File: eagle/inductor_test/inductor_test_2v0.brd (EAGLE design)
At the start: 25.4 x 25.4 mm, 43 parts, among them U1 OPA2369, U3 SC70, U4 SOT-23-6, U5 TSSOP-14

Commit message: added all components for inductor inspector
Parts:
- removed U$1: (no value), powerfilm:NEMA_1-15_TIGHT
- added C15: (no value), rcl:C0402
- added R20, R21, R22, R23: (no value), rcl:R0402
- added TP1, TP10, TP11, TP12, TP13, TP14, TP2, TP3, TP4, TP5, TP6, TP7, TP8, TP9: TP_MULT, skyspecs:TP_MULT
- added U$2: (no value), powerfilm:NEMA_F2
- added U2: OPA2369, powerfilm:SOT-23-8
- C3: device rcl:C0603 -> rcl:C0402
- moved C2 174.2 mm to (50.8, 6.11), turned to 180 degrees
- moved R5 148.3 mm to (12.7, 3.81), turned to 270 degrees
- moved C1 142.5 mm to (-1.27, 5.08), turned to 90 degrees
- moved R4 127.5 mm to (3.81, -6.35), turned to 90 degrees
- moved R2 123.8 mm to (-1.27, 0.00), turned to 90 degrees
- moved R3 123.5 mm to (2.54, -6.35), turned to 90 degrees
- moved R7 105.1 mm to (50.8, 7.38), turned to 180 degrees
- moved U3 104.7 mm to (50.8, 10.2)
- moved R6 103.1 mm to (50.8, 8.57)
- moved C3 103.0 mm to (51.4, 11.7), turned to 180 degrees
- moved L1 8.89 mm to (4.45, 5.08), turned to 226.6 degrees
- moved L2 7.21 mm to (3.61, 1.27), turned to 262.9 degrees
- moved L3 7.11 mm to (3.56, -2.54), turned to 284.7 degrees
- moved L4 4.06 mm to (2.03, 4.83), turned to 255.1 degrees
- moved L5 3.05 mm to (1.52, 0.00)
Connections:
- new net N$13: R22.1, R23.2, U2.P5
- new net N$16: R20.2, R21.1, U2.P3
- net +3V3: now also C15.1, R21.2, R22.2, U2.P8
- net GND: now also C15.2, R20.1, R23.1, TP10.P$1, TP11.P$1, TP12.P$1, TP13.P$1, TP14.P$1, TP9.P$1, U2.P4
- net OUT1_SC70: now also TP1.P$1
- net OUT1_SOT23: now also TP3.P$1
- net OUT1_TSSOP14: now also TP5.P$1
- net OUT2_SC70: now also TP2.P$1
- net OUT2_SOT23: now also TP4.P$1
- net OUT2_TSSOP14: now also TP6.P$1
- net VREF_1V65: now also TP7.P$1, U2.P1, U2.P2
- net VREF_V054: now also TP8.P$1, U2.P6, U2.P7
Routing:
- net L1P2: track 42.8 -> 0.00 mm
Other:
- board size 25.4 x 25.4 mm -> 25.4 x 50.8 mm
- board text removed: "1"
- board text removed: "10"
- board text removed: "11"
- board text removed: "12"
- board text removed: "13"
- board text removed: "14"
- board text removed: "15"
- board text removed: "2"
- board text removed: "3"
- board text removed: "4"
- board text removed: "5"
- board text removed: "6"
- board text removed: "7"
- board text removed: "8"
- board text removed: "9"
- board text removed: "CONTROL"
- board text removed: "LOAD"
- board text removed: "Layout:"

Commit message: all components added for inductor inspector
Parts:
- removed TP14: TP_MULT, skyspecs:TP_MULT
- added C16: 22pF, rcl:C0402_SM
- added C17: 4.7uF, rcl:C0402_SM
- added C18, C19: 0.1uF, rcl:C0402_SM
- added C20, C21: 22uF, rcl:C0603_SM
- added C22: 0.1uF, rcl:C0603
- added J1: MA02-1, con-lstb:MA02-1_MOLEX-TH
- added L6: 10uH, rcl:L0805
- added R24: 560k, rcl:R0402_SM
- added R25: 180k, rcl:R0402_SM
- added R26: 1 1%, rcl:R0603_SM
- added R27, R28: 10k, rcl:R0603
- added R29, R30: 10, rcl:R0603
- added TP16: TP_MULT, skyspecs:TP_MULT
- added U6: TPS62122, powerfilm:WDFN-6
- added U7: MAX9910, powerfilm:SC70-5
- C14, C4, C5: device rcl:C0603 -> rcl:C0402
- moved TP9 281.2 mm to (35.6, 10.8)
- moved TP12 280.6 mm to (35.6, -8.89)
- moved TP11 278.5 mm to (35.6, -4.76)
- moved TP10 276.3 mm to (35.6, -0.64)
- moved TP13 275.7 mm to (35.6, -20.3)
- moved TP4 243.3 mm to (35.6, 3.17)
- moved TP2 242.1 mm to (35.6, 14.6)
- moved TP3 240.9 mm to (35.6, 6.99)
- moved TP1 239.6 mm to (35.6, 18.4)
- moved TP8 237.8 mm to (35.6, -27.9)
- moved TP6 236.6 mm to (35.6, -16.5)
- moved TP7 235.4 mm to (35.6, -24.1)
- moved TP5 234.2 mm to (35.6, -12.7)
- moved C14 213.4 mm to (27.0, 0.48), turned to 270 degrees
- moved C12 204.8 mm to (28.5, 6.03)
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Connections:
- new net N$19: C16.2, R24.1, R25.2, U6.P3
- new net N$20: L6.2, U6.P1
- new net N$21: R28.1, R29.2, U7.P1
- new net N$22: R27.1, R30.2, U7.P3
- new net N$23: R27.2, TP16.P$1, U7.P4
- new net VCC: C17.1, C18.1, J1.P1, U6.P4, U6.P5
- new net VS+: C16.1, C19.1, C20.1, L6.1, R24.2, R26.1, R29.1, U6.P2
- net +3V3: now also C21.1, C22.1, R26.2, R30.1, U7.P5
- net GND: now also C17.2, C18.2, C19.2, C20.2, C21.2, C22.2, J1.P2, R25.1, R28.2, U6.P6, U6.PAD, U7.P2; no longer TP14.P$1
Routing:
- added copper zone on layer 1, net GND
- added copper zone on layer 16, net GND
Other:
- outline, holes or cut-outs redrawn

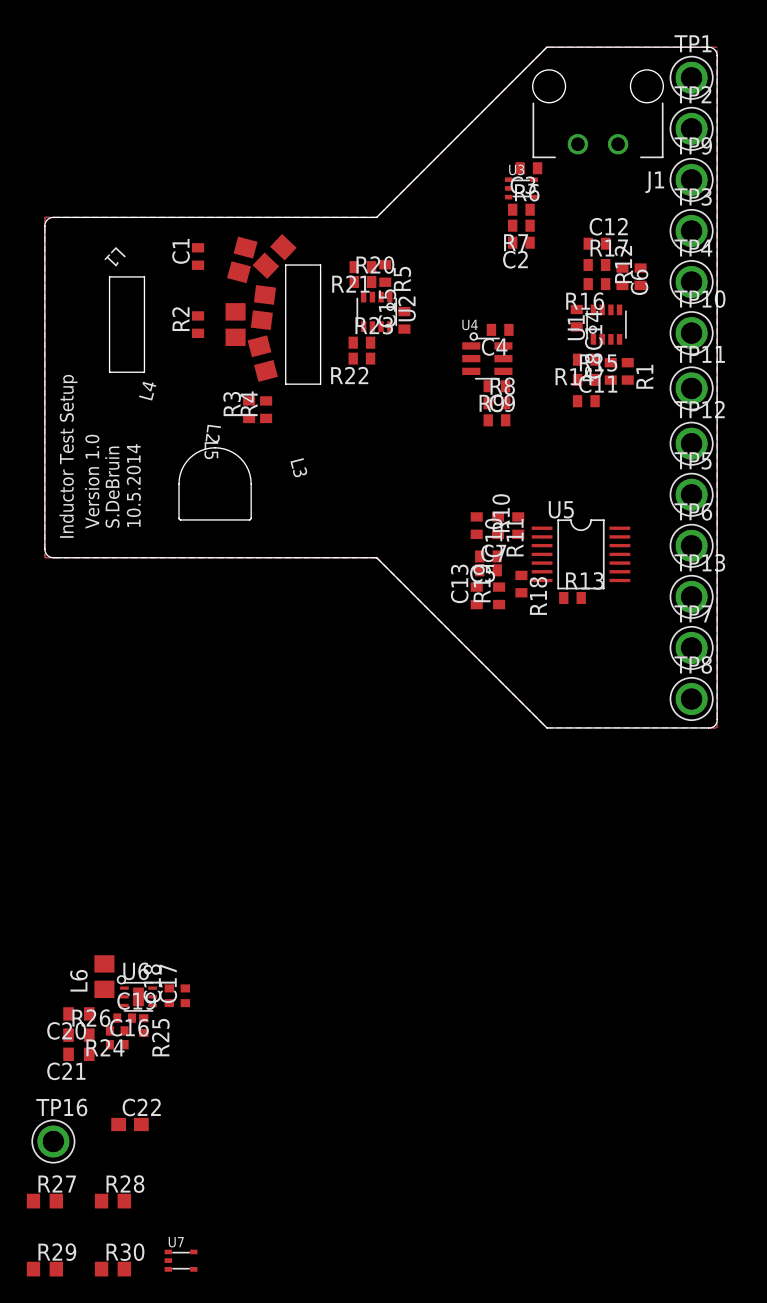
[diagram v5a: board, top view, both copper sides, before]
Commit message: 23 airwires left
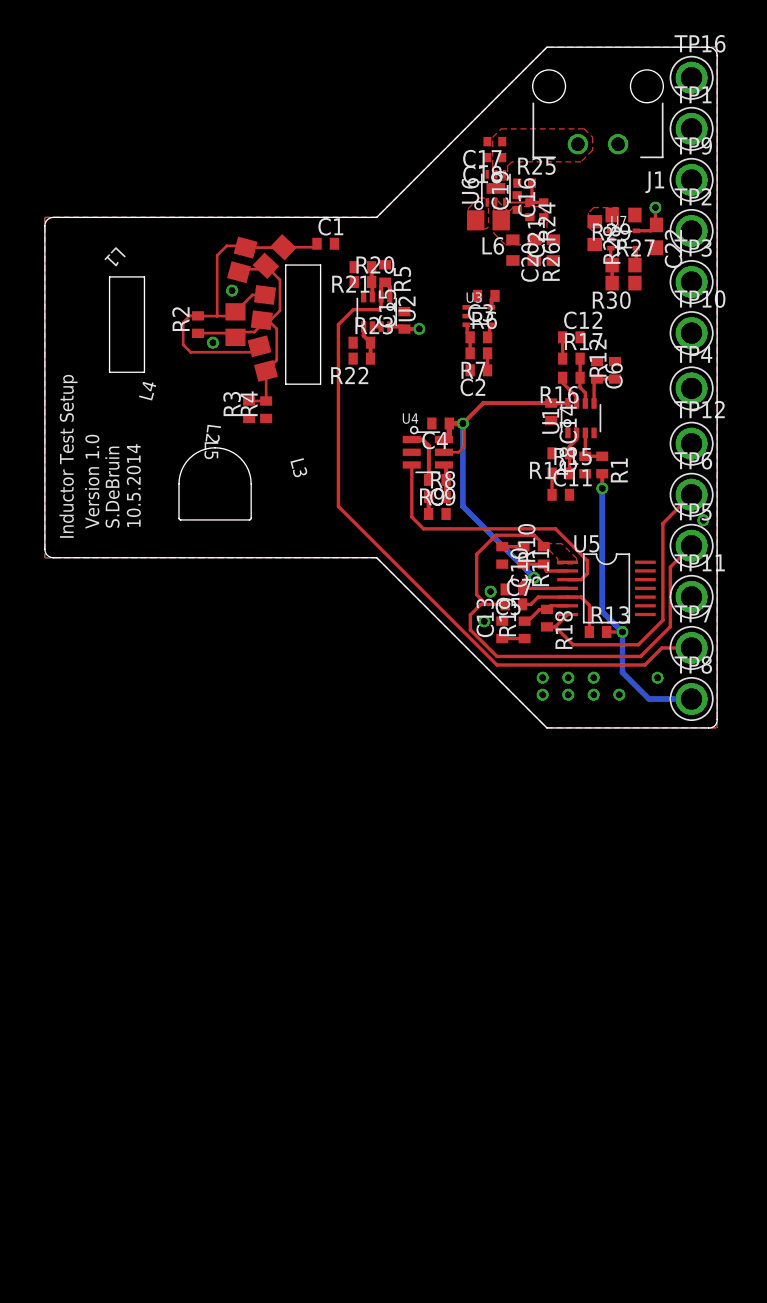
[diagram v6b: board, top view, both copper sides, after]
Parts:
- removed TP13: TP_MULT, skyspecs:TP_MULT
- moved TP16 92.6 mm to (35.6, 18.4)
- moved R29 89.7 mm to (30.5, 8.18), turned to 180 degrees
- moved U7 83.0 mm to (30.5, 6.35)
- moved R30 82.9 mm to (30.5, 3.10), turned to 180 degrees
- moved R27 82.1 mm to (30.5, 4.45)
- moved R28 80.7 mm to (28.3, 6.83), turned to 270 degrees
- moved C22 77.0 mm to (32.9, 6.59), turned to 270 degrees
- moved C16 70.0 mm to (24.5, 8.57), turned to 90 degrees
- moved C21 69.7 mm to (25.2, 5.56), turned to 90 degrees
- moved R25 69.0 mm to (23.1, 10.6), turned to 0 degrees
- moved R24 68.6 mm to (23.5, 8.57), turned to 270 degrees
- moved C17 67.8 mm to (20.9, 13.7), turned to 180 degrees
- moved R26 67.7 mm to (23.8, 5.56), turned to 270 degrees
- moved C19 67.5 mm to (22.5, 9.11), turned to 90 degrees
- moved C18 67.1 mm to (20.9, 12.5), turned to 180 degrees
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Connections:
- net GND: no longer TP13.P$1
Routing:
- net VREF_1V65: track 0.00 -> 52.3 mm
- net +3V3: track 0.00 -> 39.2 mm, vias 0 -> 4
- net OUT1_TSSOP14: track 0.00 -> 37.5 mm
- net N$4: track 0.00 -> 27.2 mm
- net VREF_V054: track 0.00 -> 23.3 mm, vias 0 -> 2
- net L1P2: track 0.00 -> 21.6 mm
- net OUT2_TSSOP14: track 0.00 -> 21.5 mm
- net L_SIG: track 0.00 -> 21.0 mm
- net N$12: track 0.00 -> 7.46 mm
- net N$19: track 0.00 -> 4.42 mm
- net OUT1_SOT23: track 0.00 -> 4.02 mm
- net N$17: track 0.00 -> 3.69 mm
- net N$8: track 0.00 -> 3.64 mm
- net N$14: track 0.00 -> 3.52 mm
- net N$9: track 0.00 -> 3.26 mm
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- added copper zone on layer 1, net N$20
- added copper zone on layer 1, net N$21
- added copper zone on layer 1, net OUT1_TSSOP14
- added copper zone on layer 1, net OUT2_TSSOP14
- added copper zone on layer 1, net VCC
- added copper zone on layer 1, net VS+

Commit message: finished basic design, about to add stuff!
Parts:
- moved C12 2.93 mm to (24.7, -3.17), turned to 270 degrees
- moved C2 2.64 mm to (21.5, -1.51), turned to 90 degrees
- moved R29 1.23 mm to (29.6, 9.05), turned to 270 degrees
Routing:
- net +3V3: track 39.2 -> 114.9 mm, vias 4 -> 7
- net OUT1_SC70: track 1.06 -> 41.3 mm, vias 0 -> 2
- net VREF_V054: track 23.3 -> 56.1 mm, vias 2 -> 5
- net OUT1_SOT23: track 4.02 -> 35.6 mm
- net L_SIG: track 21.0 -> 49.5 mm
- net OUT2_SC70: track 0.00 -> 23.8 mm, vias 0 -> 1
- net N$23: track 1.30 -> 16.5 mm
- net OUT2_SOT23: track 2.35 -> 12.4 mm
- net VS+: track 0.00 -> 5.86 mm
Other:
- board text added: "6.30.2015"
- board text added: "Inductor Test System"
- board text added: "Version 2.0"
- board text removed: "10.5.2014"
- board text removed: "Inductor Test Setup"
- board text removed: "Version 1.0"

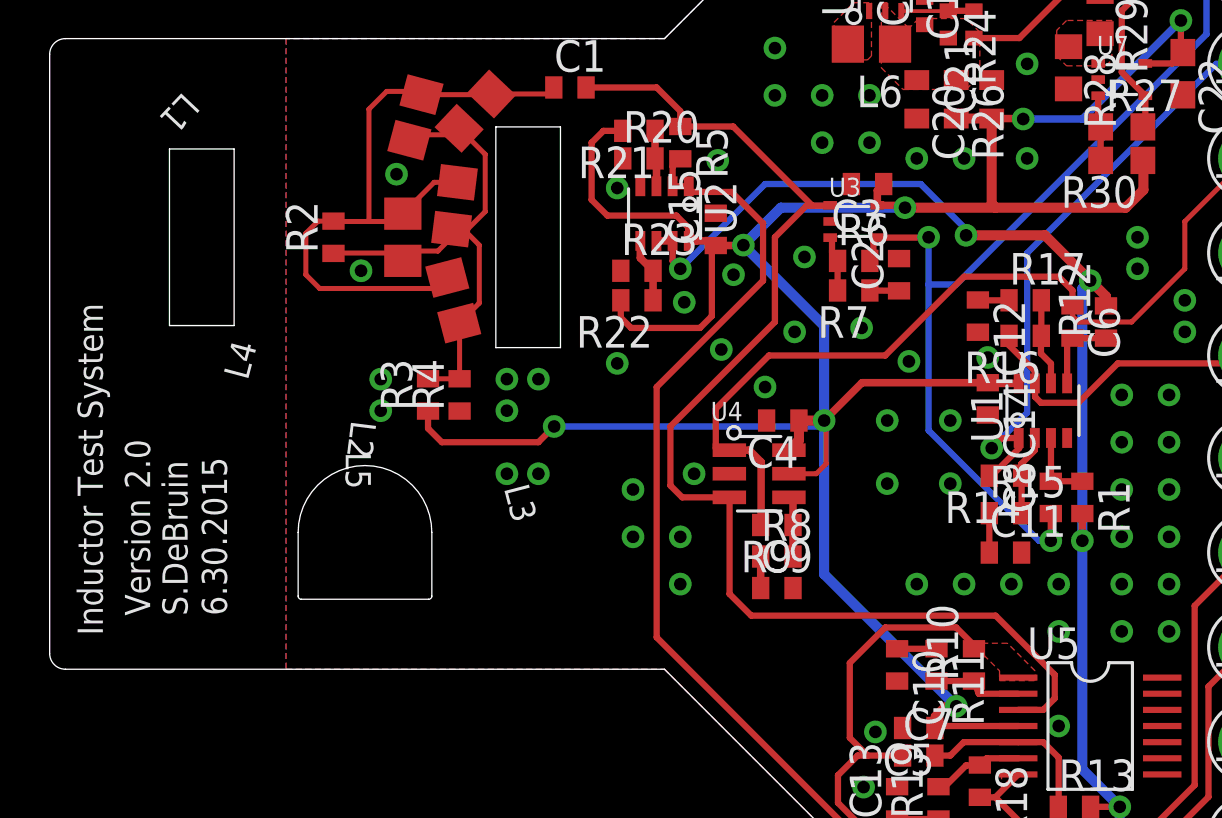
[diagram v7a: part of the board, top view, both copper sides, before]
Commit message: added pogo pin to inductor test board
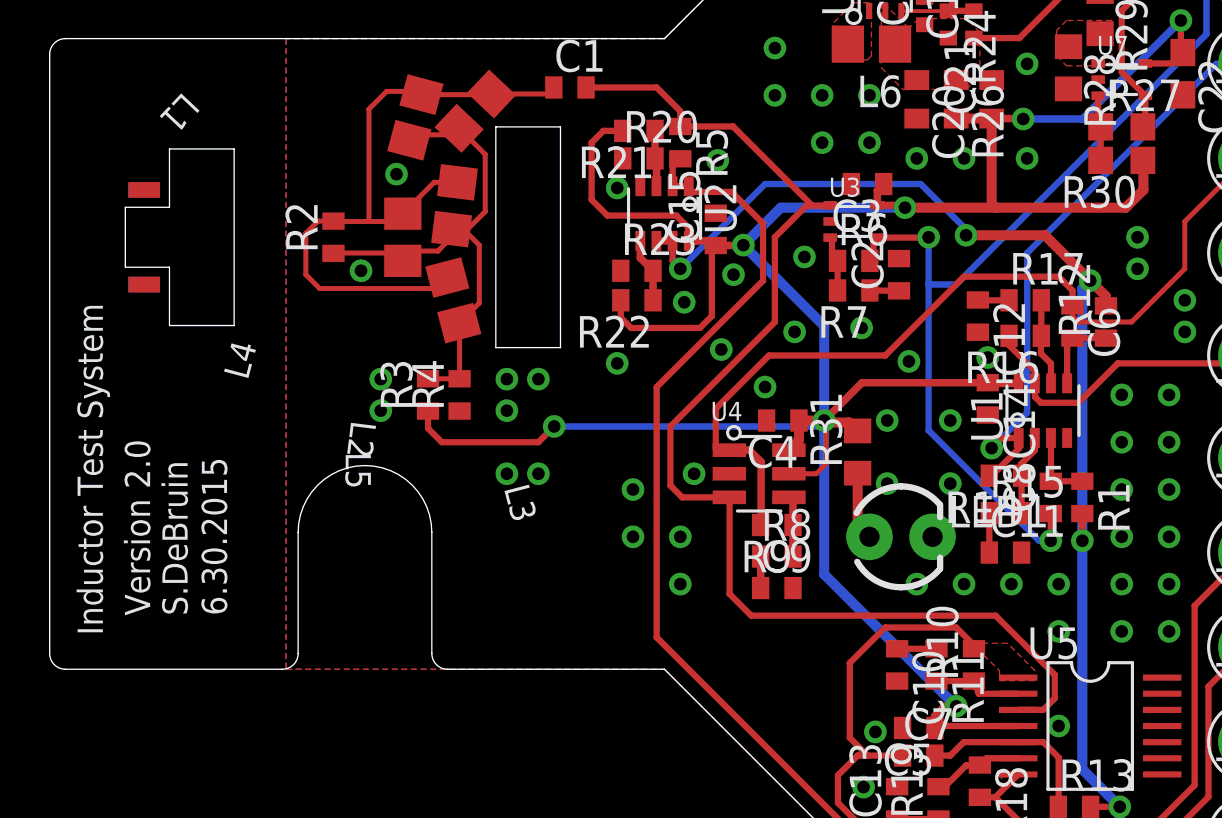
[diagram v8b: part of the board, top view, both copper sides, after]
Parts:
- added LED1: (no value), SparkFun-LED:LED3MM
- added R31: (no value), rcl:R0603
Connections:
- new net N$24: LED1.A, R31.1
- net +3V3: now also R31.2
- net GND: now also LED1.K
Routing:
- net N$24: track 0.00 -> 2.76 mm
- net +3V3: track 114.9 -> 116.3 mm
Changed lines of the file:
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@@
 <element name="R29" library="rcl" package="R0603" value="10" x="29.606875" y="9.04875" rot="R270"/>
 <element name="R30" library="rcl" package="R0603" value="10" x="30.48" y="3.095625" rot="R180"/>
+<element name="R31" library="rcl" package="R0603" value="" x="19.84375" y="-8.651875" rot="R90"/>
+<element name="LED1" library="SparkFun-LED" package="LED3MM" value="" x="21.59" y="-12.065"/>
 </elements>
 <signals>
@@
 <wire x1="13.0175" y1="0.396875" x2="13.0175" y2="0.17" width="0.254" layer="1"/>
 <wire x1="13.0175" y1="0.17" x2="13.335" y2="-0.1475" width="0.254" layer="1"/>
+<contactref element="R31" pad="2"/>
+<wire x1="18.57375" y1="-7.46125" x2="19.503125" y2="-7.46125" width="0.4064" layer="1"/>
+<wire x1="19.503125" y1="-7.46125" x2="19.84375" y2="-7.801875" width="0.4064" layer="1"/>
 </signal>
 <signal name="GND">
@@
 <via x="17.30375" y="-3.81" extent="1-16" drill="0.508"/>
 <via x="27.94" y="-19.685" extent="1-16" drill="0.508"/>
+<contactref element="LED1" pad="K"/>
 </signal>
 <signal name="L_SIG">
@@
 <wire x1="35.56" y1="17.78" x2="35.56" y2="18.415" width="0.254" layer="1"/>
 </signal>
+<signal name="N$24">
+<contactref element="R31" pad="1"/>
+<contactref element="LED1" pad="A"/>
+<wire x1="19.84375" y1="-9.501875" x2="19.84375" y2="-11.58875" width="0.4064" layer="1"/>
+<wire x1="19.84375" y1="-11.58875" x2="20.32" y2="-12.065" width="0.4064" layer="1"/>
+</signal>
 </signals>
